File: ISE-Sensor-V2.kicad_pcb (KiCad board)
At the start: 4 copper layers, 17 x 45.8 mm, 44 parts, among them CN1 BM04B-SRSS-TB(LF)(SN), U12 ADS122C04IRTER, U14 OPA928, U16 TPS7A2025PDBVR, U17 LM2776, U18 TPS72325DBV, U5 ADM3260

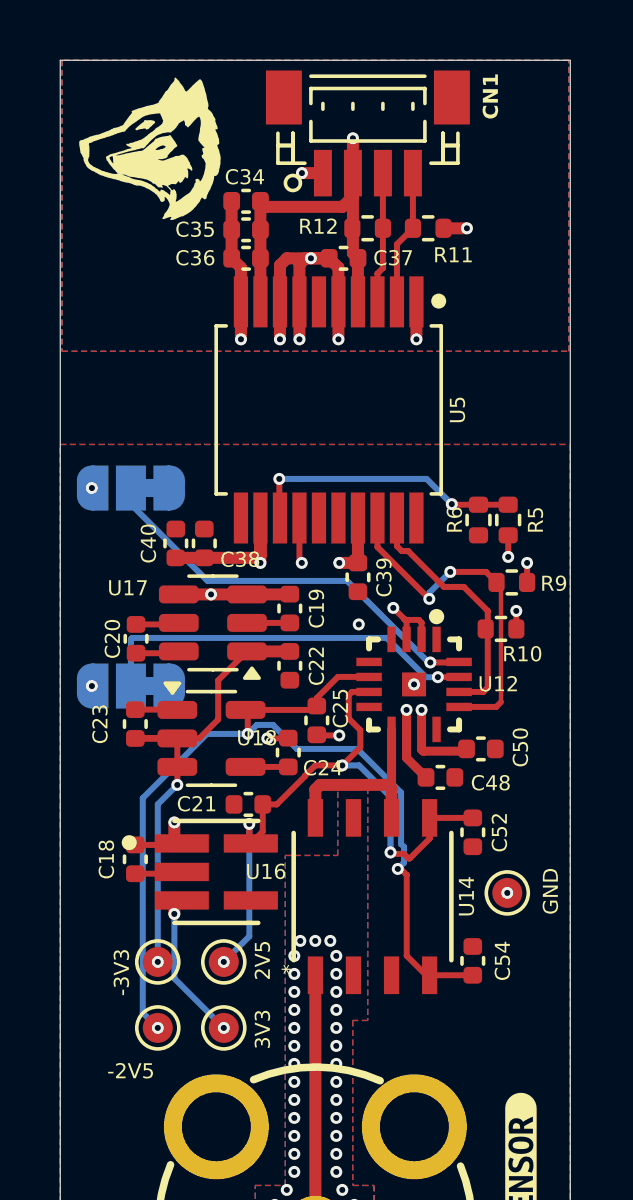
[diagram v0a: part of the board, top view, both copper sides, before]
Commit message: Add output images
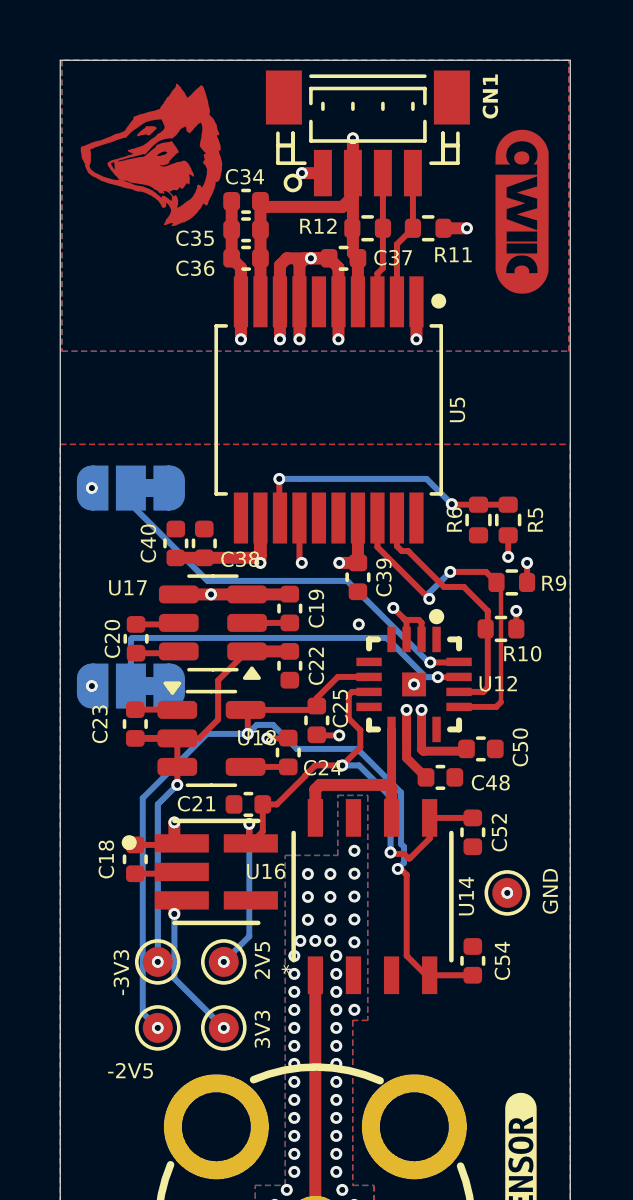
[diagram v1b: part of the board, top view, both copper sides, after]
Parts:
- removed the G*** at (126.2, 79.6)
- added G***: LOGO, Personal:WSS_LOGO_5mm_copper, F.Cu at (126.2, 79.8)
- added G***: LOGO, SparkFun-Qwiic:qwiic_5.5mm_Copper_No_Mask, F.Cu at (138.7, 81.7)
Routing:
- net /ORP/GRD: vias 43 -> 55

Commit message: Update images
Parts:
- moved C34 78.8 mm to (66.1, 34.4)
- moved C35 78.8 mm to (66.1, 35.4)
- moved C36 78.8 mm to (66.1, 36.3)
- moved C37 78.8 mm to (69.3, 36.3)
- moved C40 78.8 mm to (63.7, 45.8)
- moved C52 78.8 mm to (73.6, 55.5)
- moved C54 78.8 mm to (73.6, 59.7)
- moved G*** 78.8 mm to (75.3, 34.8)
- moved R10 78.8 mm to (74.6, 48.7)
- moved R12 78.8 mm to (70.1, 35.3)
- moved R6 78.8 mm to (73.8, 45.0)
- moved C18 78.8 mm to (62.4, 56.4)
- moved C20 78.8 mm to (62.4, 49.0)
- moved C23 78.8 mm to (62.4, 51.8)
- moved C24 78.8 mm to (67.5, 52.8)
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
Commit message: Updates
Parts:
- removed RF3: ORP Sensor, EasyEDA:BNC-TH_DOSIN-801-0051
- added C49: 100nF, Capacitor_SMD:C_0402_1005Metric, F.Cu at (37.0, 42.2)
- added C51: 10uF, Capacitor_SMD:C_0402_1005Metric, F.Cu at (24.5, 42.8)
- added C53: 50uF, Capacitor_SMD:C_0402_1005Metric, F.Cu at (22.7, 53.0)
- added C55: 1uF, Capacitor_SMD:C_0402_1005Metric, F.Cu at (22.7, 51.8)
- added C56: 1uF, Capacitor_SMD:C_0402_1005Metric, F.Cu at (22.7, 54.0)
- added C57: 100nF, Capacitor_SMD:C_0402_1005Metric, F.Cu at (34.3, 44.5)
- added ISE1: DOSIN-801-0080, EasyEDA:BNC-TH_DOSIN-801-0080, F.Cu at (30.0, 59.2)
- added U1: REF5025IDR, EasyEDA:SOIC-8_L4.9-W3.9-P1.27-LS6.0-BL, F.Cu at (25.1, 47.3)
- added kibuzzard-67B4F71A: G***, kibuzzard-67B4F71A, F.Cu at (36.4, 26.7)
- moved kibuzzard-67AA55DF 52.7 mm to (23.4, 58.8)
- moved TP6 49.2 mm to (25.4, 33.3), turned to -90 degrees
- moved TP12 45.9 mm to (37.7, 30.4), turned to -90 degrees
- moved R9 44.7 mm to (32.6, 32.7), turned to 90 degrees
- moved C18 44.7 mm to (22.5, 36.1)
- moved U16 44.7 mm to (25.2, 36.6)
- moved R10 43.8 mm to (34.2, 31.6)
- moved TP10 43.5 mm to (29.8, 34.7), turned to -90 degrees
- moved R5 43.5 mm to (34.1, 29.8)
- moved R6 43.5 mm to (33.1, 29.8)
- moved C37 43.0 mm to (29.0, 21.4)
- moved R11 42.9 mm to (32.0, 20.4)
- moved R12 42.9 mm to (29.9, 20.4)
- moved C34 42.8 mm to (25.9, 19.7)
- moved C35 42.8 mm to (25.9, 20.7)
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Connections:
- net /ORP/ISO_-3V3 renamed /ORP/PP_ISO_NEG_3V3
- C18 pad 1: /ISO_3V3 -> /PP_ISO_3V3
- C19 pad 1: /ISO_3V3 -> /PP_ISO_3V3
- C21 pad 1: /ORP/ISO_2V5 -> /ORP/PP_ISO_2V5
- C25 pad 2: /ORP/ISO_-2V5 -> /ORP/PP_ISO_NEG_2V5
- C38 pad 1: /ISO_3V3 -> /PP_ISO_3V3
- C39 pad 1: /ISO_3V3 -> /PP_ISO_3V3
- C40 pad 1: /ISO_3V3 -> /PP_ISO_3V3
- C48 pad 1: /ISO_3V3 -> /PP_ISO_3V3
- C50 pad 1: /ISO_3V3 -> /ORP/PP_ISO_2V5
- C52 pad 2: /ORP/ISO_2V5 -> /ORP/PP_ISO_2V5
- C54 pad 2: /ORP/ISO_-2V5 -> /ORP/PP_ISO_NEG_2V5
- JP3 pad 3: /ISO_3V3 -> /PP_ISO_3V3
- JP4 pad 3: /ISO_3V3 -> /PP_ISO_3V3
- R10 pad 2: /ISO_3V3 -> /PP_ISO_3V3
- R5 pad 2: /ISO_3V3 -> /PP_ISO_3V3
- R9 pad 1: /ISO_3V3 -> /PP_ISO_3V3
- TP10 pad 1: /ORP/ISO_2V5 -> /ORP/PP_ISO_2V5
- TP11 pad 1: /ORP/ISO_-2V5 -> /ORP/PP_ISO_NEG_2V5
- TP6 pad 1: /ISO_3V3 -> /PP_ISO_3V3
- U12 pad 10: /ISO_3V3 -> /ORP/PP_ISO_2V5
- U12 pad 11: /ISO_3V3 -> /PP_ISO_3V3
- U12 pad 3: /ISO_GND -> /ORP/PP_ISO_NEG_2V5
- U12 pad 5: unconnected-(U12-AIN2-Pad5) -> /ORP/TEMP
- U12 pad 6: /ORP/ISO_-2V5 -> unconnected-(U12-REFN-Pad6)
- U12 pad 7: /ORP/ISO_2V5 -> /ORP/PP_ISO_REF_2V5
- U14 pad 4: /ORP/ISO_-2V5 -> /ORP/PP_ISO_NEG_2V5
- U14 pad 5: /ORP/ISO_2V5 -> /ORP/PP_ISO_2V5
- U16 pad 1: /ISO_3V3 -> /PP_ISO_3V3
- U16 pad 3: /ISO_3V3 -> /PP_ISO_3V3
- U16 pad 5: /ORP/ISO_2V5 -> /ORP/PP_ISO_2V5
- U17 pad 3: /ISO_3V3 -> /PP_ISO_3V3
- U17 pad 4: /ISO_3V3 -> /PP_ISO_3V3
- U18 pad 5: /ORP/ISO_-2V5 -> /ORP/PP_ISO_NEG_2V5
- U5 pad 12: /ISO_3V3 -> /PP_ISO_3V3
- U5 pad 17: /ISO_3V3 -> /PP_ISO_3V3
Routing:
- net /PP_ISO_3V3: track 0.00 -> 34.2 mm, vias 0 -> 12
- net /ORP/ISO_-2V5: track 32.2 -> 0.00 mm, vias 3 -> 0
- net /ISO_GND: track 9.82 -> 38.7 mm, vias 7 -> 22
- net /ISO_3V3: track 25.7 -> 0.00 mm, vias 13 -> 0
- net /ORP/PP_ISO_2V5: track 0.00 -> 23.0 mm, vias 0 -> 2
- net /ORP/PP_ISO_NEG_2V5: track 0.00 -> 23.0 mm, vias 0 -> 2
- net /ORP/ISO_2V5: track 21.4 -> 0.00 mm, vias 4 -> 0
- net /ORP/PP_ISO_REF_2V5: track 0.00 -> 17.6 mm
- net /ORP/TEMP: track 0.00 -> 13.6 mm
- net /ORP/ISO_SCL: track 8.43 -> 20.7 mm, vias 0 -> 2
- net /ORP/ISO_SDA: track 12.0 -> 21.5 mm
- net /A0: track 13.1 -> 6.25 mm
- net /A1: track 13.7 -> 8.70 mm
- net GND: track 17.3 -> 13.5 mm, vias 7 -> 8
- net /ORP/PP_ISO_NEG_3V3: track 16.2 -> 13.6 mm, vias 2 -> 0
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- added copper zone on In2.Cu, net /PP_ISO_3V3
- removed copper zone on In2.Cu, net /ISO_3V3
- removed copper zone on B.Cu, net /ORP/GRD
- removed copper zone on In2.Cu, net /ORP/GRD
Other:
- board size 17 x 45.8 mm -> 20 x 50 mm
